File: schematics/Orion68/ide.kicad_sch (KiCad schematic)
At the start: 2 parts, among them J5 Euro96pin, U31 GAL20V8

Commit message: Implemented new picoVGA V2
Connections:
- net VERMELHO: now reaches U31.6 (I)
- net VERMELHO: now also J5.58
- net PRETO: now reaches J5.57
- net /DTACK_PVGA: now reaches J5.59
- net /DTACK_PVGA: now also U31.5 (I)
- net /CS_MULTIIO renamed AMARELO
- net AMARELO: now also J5.61
- net /DTACK renamed LILAS
- net /DTACK_AUTO renamed VERDE
- net /DTACK_PICOVGA renamed MARRON
- net MARRON: now also U31.4 (I); no longer U31.5 (I)
- removed net /DTACK_SMIO: J5.61, U31.4 (I)
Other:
- note added: "LILAS"

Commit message: Implementede 68681, led blink,uart to test
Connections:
- net /CS_DUART: now reaches J5.56
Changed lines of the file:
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@@
+	(wire
+		(pts
+			(xy 123.19 78.74) (xy 128.27 78.74)
+		)
+		(stroke
+			(width 0)
+			(type default)
+		)
+	)
 	(wire
 		(pts
@@
 		(pts
 			(xy 134.62 27.94) (xy 133.35 27.94)
+		)
+		(stroke
+			(width 0)
+			(type default)
+		)
+	)
+	(wire
+		(pts
+			(xy 128.27 78.74) (xy 128.27 128.27)
+		)
+		(stroke
+			(width 0)
+			(type default)
+		)
+	)
+	(wire
+		(pts
+			(xy 107.95 128.27) (xy 128.27 128.27)
 		)
 		(stroke
@@
 		)
 	)
-	(label "{slash}DTACK_68681"
+	(label "{slash}DTACK_DUART"
 		(at 107.95 125.73 180)
 		(effects
@@
 		(effects
 			(font
+				(size 1.27 1.27)
+			)
+			(justify right bottom)
+		)
+	)
+	(label "{slash}CS_DUART"
+		(at 107.95 128.27 180)
+		(effects
+			(font

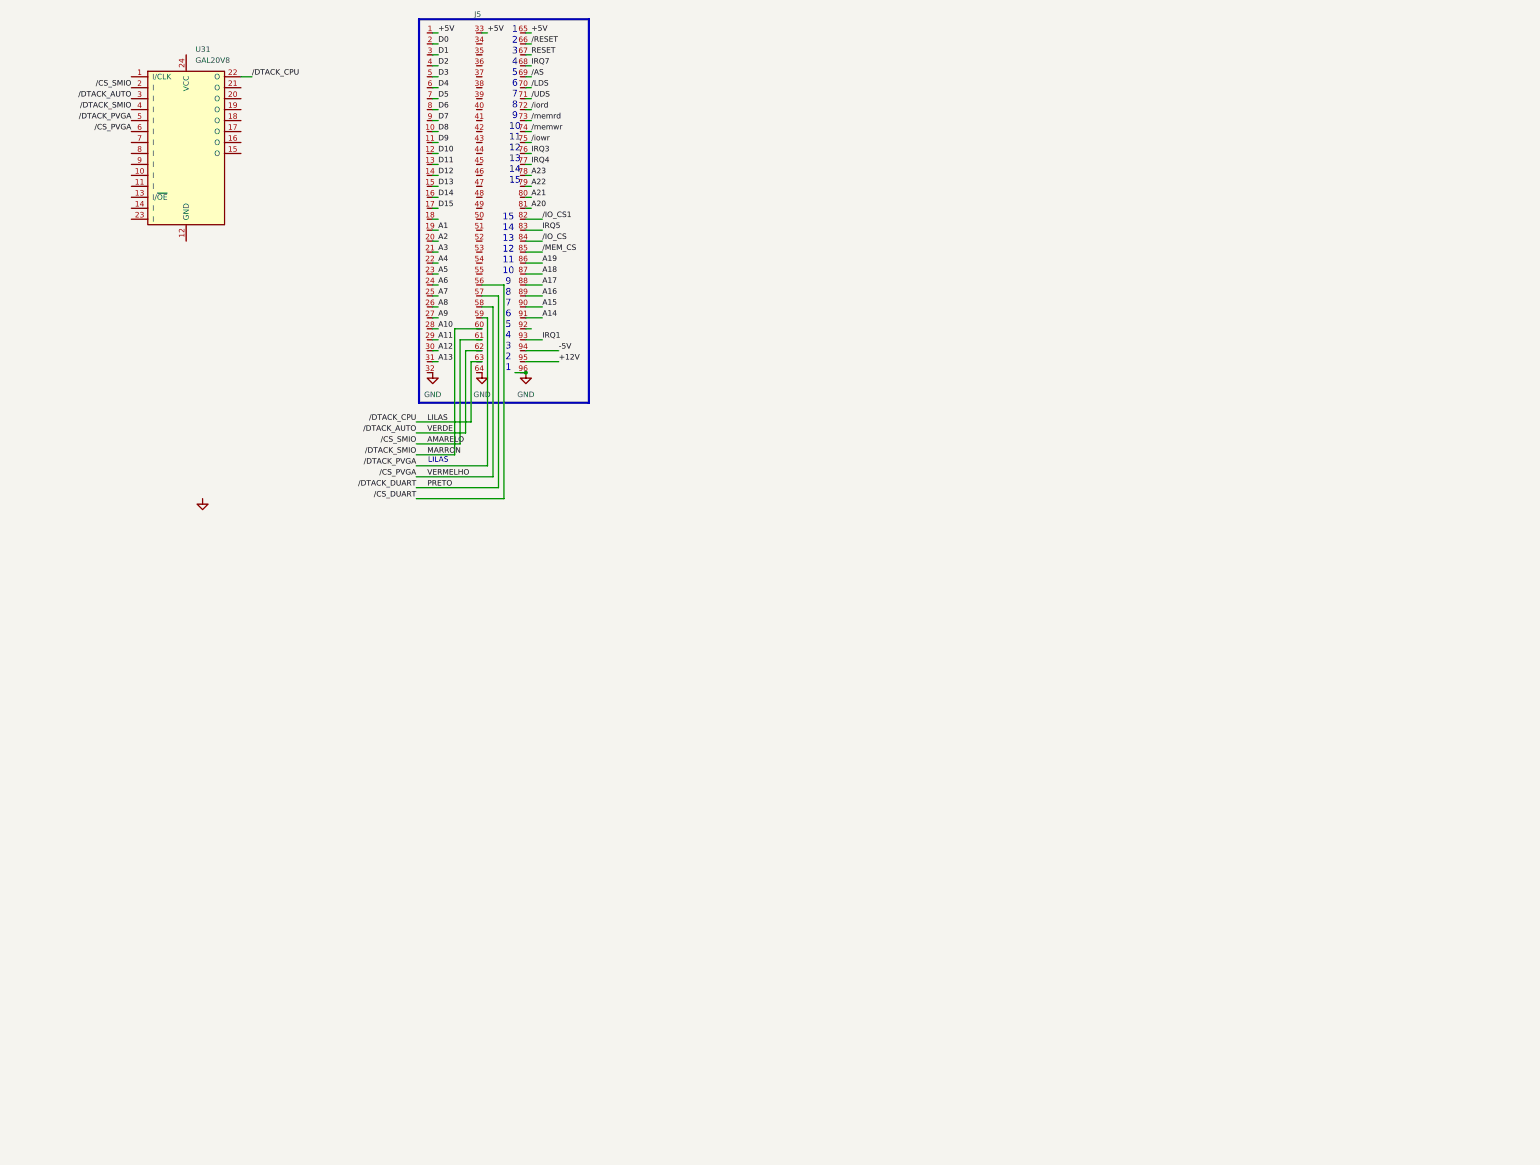
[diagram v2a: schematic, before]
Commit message: Power control implemented
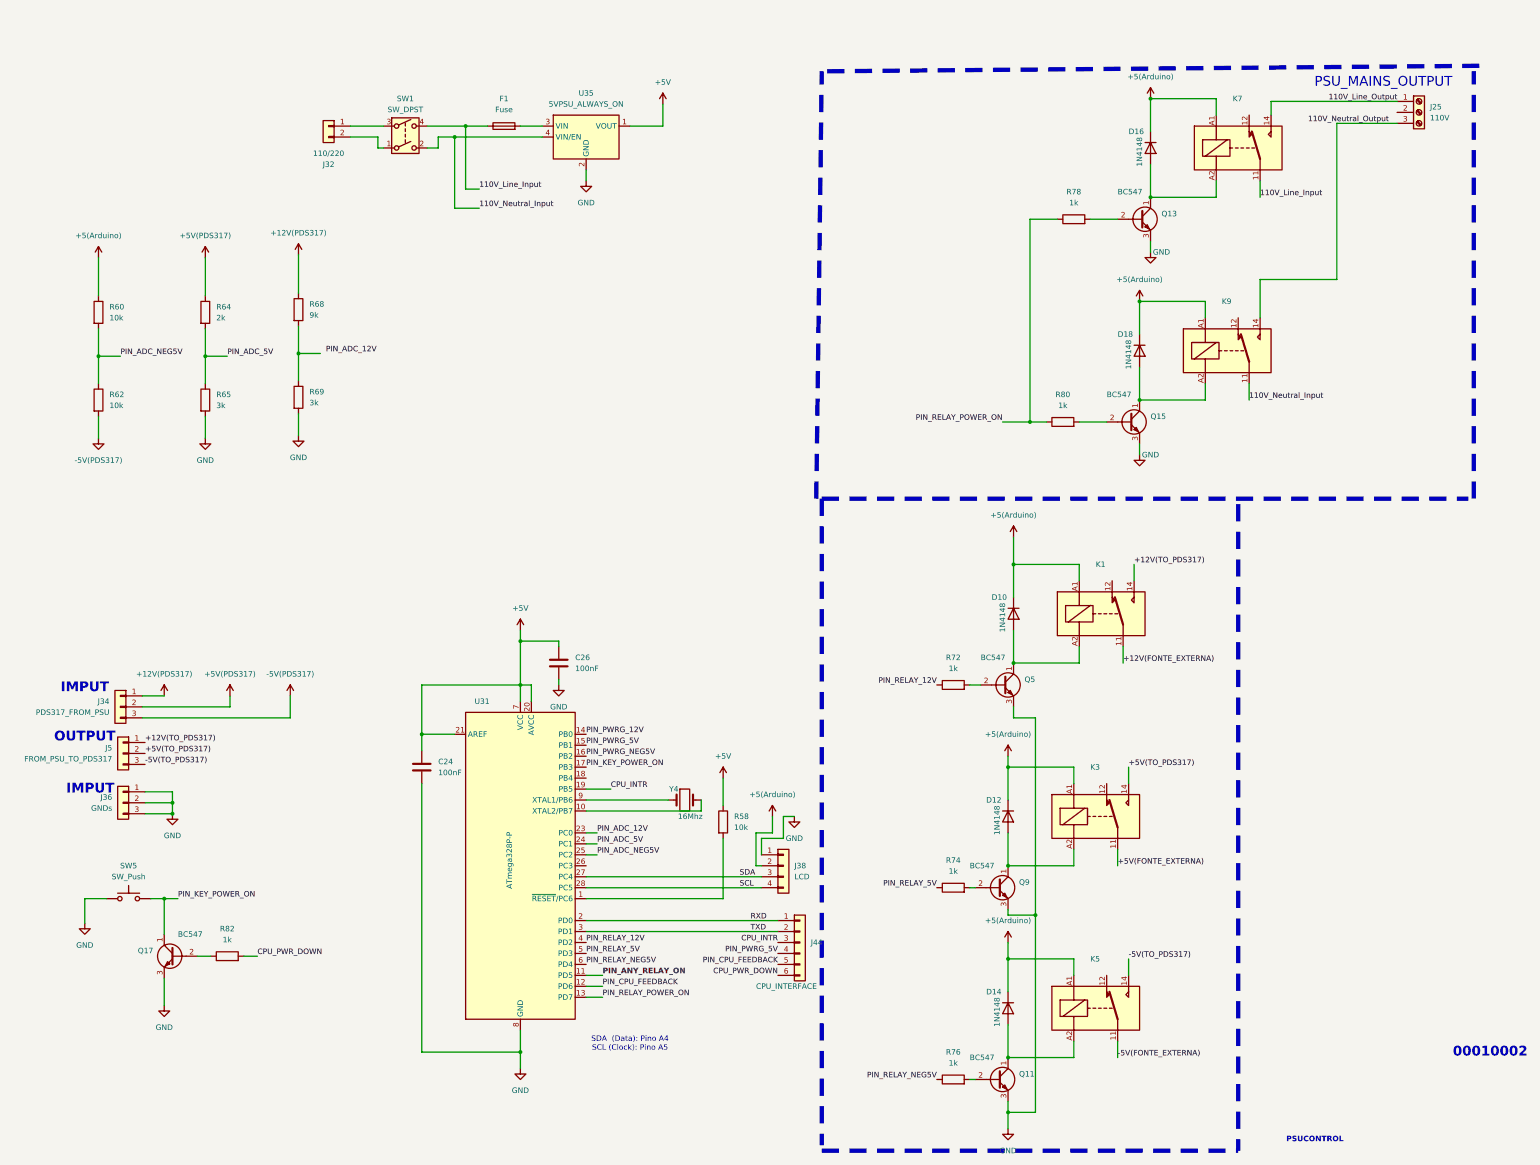
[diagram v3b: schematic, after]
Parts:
- removed J5: Euro96pin, ConnPdSilva:conn_euro96, symbol ConnPdSilva:ConnEuro96
- removed U31: GAL20V8, Package_DIP:DIP-24_W7.62mm_Socket, symbol plds:GAL20V8
- added C24, C26: 100nF, symbol Device:C
- added D10, D12, D14, D16, D18: 1N4148, Diode_THT:D_DO-35_SOD27_P7.62mm_Horizontal, symbol Diode:1N4148
- added F1: Fuse, symbol Device:Fuse
- added J25: 110V, symbol Connector:Screw_Terminal_01x03
- added J32: 110/220, symbol Connector_Generic:Conn_01x02
- added J34: PDS317_FROM_PSU, symbol Connector_Generic:Conn_01x03
- added J36: GNDs, symbol Connector_Generic:Conn_01x03
- added J38: LCD, symbol Connector_Generic:Conn_01x04
- added J44: CPU_INTERFACE, symbol Connector_Generic:Conn_01x06
- added J5: FROM_PSU_TO_PDS317, symbol Connector_Generic:Conn_01x03
- added K1, K3, K5, K7, K9: Fujitsu_FTR-LYCA005x, Relay_THT:Relay_SPDT_Fujitsu_FTR-LYCA005x_FormC_Vertical, symbol Relay:Fujitsu_FTR-LYCA005x
- added Q11, Q13, Q15, Q17, Q5, Q9: BC547, Package_TO_SOT_THT:TO-92_Inline, symbol Transistor_BJT:BC547
- added R58, R60, R62: 10k, symbol Device:R
- added R64: 2k, symbol Device:R
- added R65, R69: 3k, symbol Device:R
- added R68: 9k, symbol Device:R
- added R72, R74, R76, R78, R80, R82: 1k, symbol Device:R
- added SW1: SW_DPST, symbol Switch:SW_DPST
- added SW5: SW_Push, symbol Switch:SW_Push
- added U31: ATmega328P-P, Package_DIP:DIP-28_W7.62mm, symbol MCU_Microchip_ATmega:ATmega328P-P
- added U35: 5VPSU_ALWAYS_ON, symbol Power_Management:RT9701
- added Y4: 16Mhz, symbol Device:Crystal
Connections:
- net +5V: now also C24.1, C26.1, R58.1, U31.20 (AVCC), U31.21 (AREF), U31.7 (VCC), U35.1 (VOUT), U35.5 (VOUT)
- net GND: now also C24.2, C26.2, J36.1 (Pin_1), J36.2 (Pin_2), J36.3 (Pin_3), J38.1 (Pin_1), Q11.3 (E), Q13.3 (E), Q15.3 (E), Q17.3 (E), Q5.3 (E), Q9.3 (E), R65.2, R69.2, SW5.1, U31.22 (GND), U31.8 (GND), U35.2 (GND)
- new net: D14.2 (A), K5.A2, Q11.1 (C)
- new net: D16.2 (A), K7.A2, Q13.1 (C)
- new net: D10.2 (A), K1.A2, Q5.1 (C)
- new net: Q17.2 (B), R82.1
- new net: Q15.2 (B), R80.2
- new net: R68.2, R69.1
- new net: F1.2, U35.3 (VIN)
- new net: U31.9 (XTAL1/PB6), Y4.1
- new net: U31.10 (XTAL2/PB7), Y4.2
- new net: Q11.2 (B), R76.2
- new net: R58.2, U31.1 (~{RESET}/PC6)
- new net: D12.2 (A), K3.A2, Q9.1 (C)
- new net: Q9.2 (B), R74.2
- new net: D18.2 (A), K9.A2, Q15.1 (C)
- new net: J32.1 (Pin_1), SW1.3
- new net: J32.2 (Pin_2), SW1.1
- new net: Q5.2 (B), R72.2
- new net: Q13.2 (B), R78.2
- new net +12V(FONTE_EXTERNA): K1.11
- new net +12V(PDS317): J34.1 (Pin_1), R68.1
- new net +12V(TO_PDS317): J5.1 (Pin_1), K1.14
- new net +5(Arduino): D10.1 (K), D12.1 (K), D14.1 (K), D16.1 (K), D18.1 (K), J38.2 (Pin_2), K1.A1, K3.A1, K5.A1, K7.A1, K9.A1, R60.1
- new net +5V(FONTE_EXTERNA): K3.11
- new net +5V(PDS317): J34.2 (Pin_2), R64.1
- new net +5V(TO_PDS317): J5.2 (Pin_2), K3.14
- new net -5V(FONTE_EXTERNA): K5.11
- new net -5V(PDS317): J34.3 (Pin_3), R62.2
- new net -5V(TO_PDS317): J5.3 (Pin_3), K5.14
- new net 110V_Line_Input: F1.1, K7.11, SW1.4
- new net 110V_Line_Output: J25.1 (Pin_1), K7.14
- new net 110V_Neutral_Input: K9.11, SW1.2, U35.4 (VIN/EN)
- new net 110V_Neutral_Output: J25.3 (Pin_3), K9.14
- new net CPU_INTR: J44.3 (Pin_3), U31.19 (PB5)
- new net CPU_PWR_DOWN: J44.6 (Pin_6), R82.2
- new net PIN_ADC_12V: U31.23 (PC0)
- new net PIN_ADC_5V: R64.2, R65.1, U31.24 (PC1)
- new net PIN_ADC_NEG5V: R60.2, R62.1, U31.25 (PC2)
- new net PIN_ANY_RELAY_ON: U31.11 (PD5)
- new net PIN_CPU_FEEDBACK: J44.5 (Pin_5), U31.12 (PD6)
- new net PIN_KEY_POWER_ON: Q17.1 (C), SW5.2, U31.17 (PB3)
- new net PIN_PWRG_12V: U31.14 (PB0)
- new net PIN_PWRG_5V: J44.4 (Pin_4), U31.15 (PB1)
- new net PIN_PWRG_NEG5V: U31.16 (PB2)
- new net PIN_RELAY_12V: R72.1, U31.4 (PD2)
- new net PIN_RELAY_5V: R74.1, U31.5 (PD3)
- new net PIN_RELAY_NEG5V: R76.1, U31.6 (PD4)
- new net PIN_RELAY_POWER_ON: R78.1, R80.1, U31.13 (PD7)
- new net RXD: J44.1 (Pin_1), U31.2 (PD0)
- new net SCL: J38.4 (Pin_4), U31.28 (PC5)
- new net SDA: J38.3 (Pin_3), U31.27 (PC4)
- new net TXD: J44.2 (Pin_2), U31.3 (PD1)
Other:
- note added: "00010002"
- note added: "IMPUT"
- note added: "OUTPUT"
- note added: "PSUCONTROL"
- note added: "PSU_MAINS_OUTPUT"
- note added: "SDA (Data): Pino A4 SCL (Clock): Pino A5"
- note removed: "1 2 3 4 5 6 7 8 9 10 11 12 13 14 15"
- note removed: "15 14 13 12 11 10 9 8 7 6 5 4 3 2 1"
- note removed: "LILAS"
